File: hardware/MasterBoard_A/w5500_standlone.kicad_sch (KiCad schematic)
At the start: 1 part, among them U18 W5500

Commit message: some progress
w5500 maybe works? shuffled around some more stuff and what not
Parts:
- added C43, C47, C56: 1u, Capacitor_SMD:C_1206_3216Metric_Pad1.33x1.80mm_HandSolder, symbol Device:C_Small
- added C48, C50, C55: 220n, Capacitor_SMD:C_0805_2012Metric_Pad1.18x1.45mm_HandSolder, symbol Device:C_Small
- added C53, C69: 1n 2kV, Capacitor_SMD:C_1206_3216Metric_Pad1.33x1.80mm_HandSolder, symbol Device:C_Small
- added C54: 10u, Capacitor_SMD:C_1206_3216Metric_Pad1.33x1.80mm_HandSolder, symbol Device:C_Small
- added C57: 100n, Capacitor_SMD:C_1206_3216Metric_Pad1.33x1.80mm_HandSolder, symbol Device:C_Small
- added C58, C63, C64: 6.8n, Capacitor_SMD:C_0805_2012Metric_Pad1.18x1.45mm_HandSolder, symbol Device:C_Small
- added C59, C62, C65, C67: 10n, Capacitor_SMD:C_0805_2012Metric_Pad1.18x1.45mm_HandSolder, symbol Device:C_Small
- added C60, C68: 22n, Capacitor_SMD:C_0805_2012Metric_Pad1.18x1.45mm_HandSolder, symbol Device:C_Small
- added C66, C71, C72: 18p, Capacitor_SMD:C_0805_2012Metric_Pad1.18x1.45mm_HandSolder, symbol Device:C_Small
- added C70: 4.7u, Capacitor_SMD:C_0805_2012Metric_Pad1.18x1.45mm_HandSolder, symbol Device:C_Small
- added J10: RJ45_Amphenol_RJMG1BD3B8K1ANR, Connector_RJ:RJ45_Amphenol_RJMG1BD3B8K1ANR, symbol Connector:RJ45_Amphenol_RJMG1BD3B8K1ANR
- added NT1, NT2: NetTie_2, symbol Device:NetTie_2
- added R57: 2.4k, Resistor_SMD:R_0805_2012Metric_Pad1.20x1.40mm_HandSolder, symbol Device:R_Small_US
- added R60, R81, R82: 750, Resistor_SMD:R_1206_3216Metric_Pad1.30x1.75mm_HandSolder, symbol Device:R_Small_US
- added R62: 39k, Resistor_SMD:R_0805_2012Metric_Pad1.20x1.40mm_HandSolder, symbol Device:R_Small_US
- added R63: 3.32k, Resistor_SMD:R_0805_2012Metric_Pad1.20x1.40mm_HandSolder, symbol Device:R_Small_US
- added R64: 97.6k, Resistor_SMD:R_0805_2012Metric_Pad1.20x1.40mm_HandSolder, symbol Device:R_Small_US
- added R65, R72, R73, R78, R79: 49.9, Resistor_SMD:R_0805_2012Metric_Pad1.20x1.40mm_HandSolder, symbol Device:R_Small_US
- added R66: 4.99k, Resistor_SMD:R_1206_3216Metric_Pad1.30x1.75mm_HandSolder, symbol Device:R_Small_US
- added R67: 10k, Resistor_SMD:R_0805_2012Metric_Pad1.20x1.40mm_HandSolder, symbol Device:R_Small_US
- added R68, R80: 10, Resistor_SMD:R_1206_3216Metric_Pad1.30x1.75mm_HandSolder, symbol Device:R_Small_US
- added R69: 121, Resistor_SMD:R_0805_2012Metric_Pad1.20x1.40mm_HandSolder, symbol Device:R_Small_US
- added R70, R87: 226, Resistor_SMD:R_0805_2012Metric_Pad1.20x1.40mm_HandSolder, symbol Device:R_Small_US
- added R71, R74, R75, R76, R77: 3.3, Resistor_SMD:R_1206_3216Metric_Pad1.30x1.75mm_HandSolder, symbol Device:R_Small_US
- added R84: 12.4k, Resistor_SMD:R_0805_2012Metric_Pad1.20x1.40mm_HandSolder, symbol Device:R_Small_US
- added R85, R86: 1M, Resistor_SMD:R_0805_2012Metric_Pad1.20x1.40mm_HandSolder, symbol Device:R_Small_US
- added Y1: 25MHz, Crystal:Crystal_SMD_ECS_CSM3X-2Pin_7.6x4.1mm, symbol Device:Crystal
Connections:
- net at U18.1 (TXN): now also R72.1, R74.2
- net at U18.10 (EXRES1): now also R84.1
- net +3.3VA: now reaches U18.11 (AVDD), U18.15 (AVDD), U18.17 (AVDD), U18.21 (AVDD), U18.4 (AVDD), U18.8 (AVDD)
- net +3.3VA: now also C43.1, C47.1, C48.1, C50.1, NT1.2, R72.2, R73.2, R80.2
- net GNDA: now reaches U18.14 (AGND), U18.16 (AGND), U18.19 (AGND), U18.3 (AGND), U18.48 (AGND), U18.9 (AGND)
- net GNDA: now also C43.2, C47.2, C48.2, C50.2, C62.2, C67.2, C68.2, C69.2, C70.2, NT2.2, R84.2
- net at U18.2 (TXP): now also R73.1, R75.2
- net at U18.20 (TOCAP): now also C70.1
- net at U18.22 (1V2O): now also C65.1
- net at U18.25 (LINKLED): now also R82.1
- net at U18.27 (ACTLED): now also R81.1
- net +3.3V: now reaches U18.28 (VDD)
- net +3.3V: now also J10.L1, J10.L4, NT1.1
- net GND: now reaches U18.29 (GND)
- net GND: now also C65.2, C69.1, C71.2, C72.2, J10.R8, NT2.1
- net at U18.30 (XI/CLKIN): now also R86.1, R87.1
- net at U18.31 (XO): now also C71.1, R86.2, Y1.2
- net at U18.5 (RXN): now also R76.2, R79.2
- net at U18.6 (RXP): now also R77.2, R78.2
- new net: J10.L3, R81.2
- new net: C64.1, R77.1
- new net: C63.1, R76.1
- new net: C67.1, J10.R5 (RCT)
- new net: C68.1, J10.R4 (TCT), R80.1
- new net: C62.1, R78.1, R79.1
- new net: C63.2, J10.R3 (RD+)
- new net: C72.1, R87.2, Y1.1
- new net: J10.R1 (TD+), R74.1
- new net: C64.2, J10.R6 (RD-)
- new net: J10.R2 (TD-), R75.1
- new net: J10.L2, R82.2
- no-connect marks 0 -> 13
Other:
- note added: "- 99% chance does not meet FCC standards"
- note added: "design guide: https://docs.wiznet.io/img/design_guide/Wiznet%20Ethernet%20Design%20Guide_ENG.pdf"
- moved on the sheet: U18

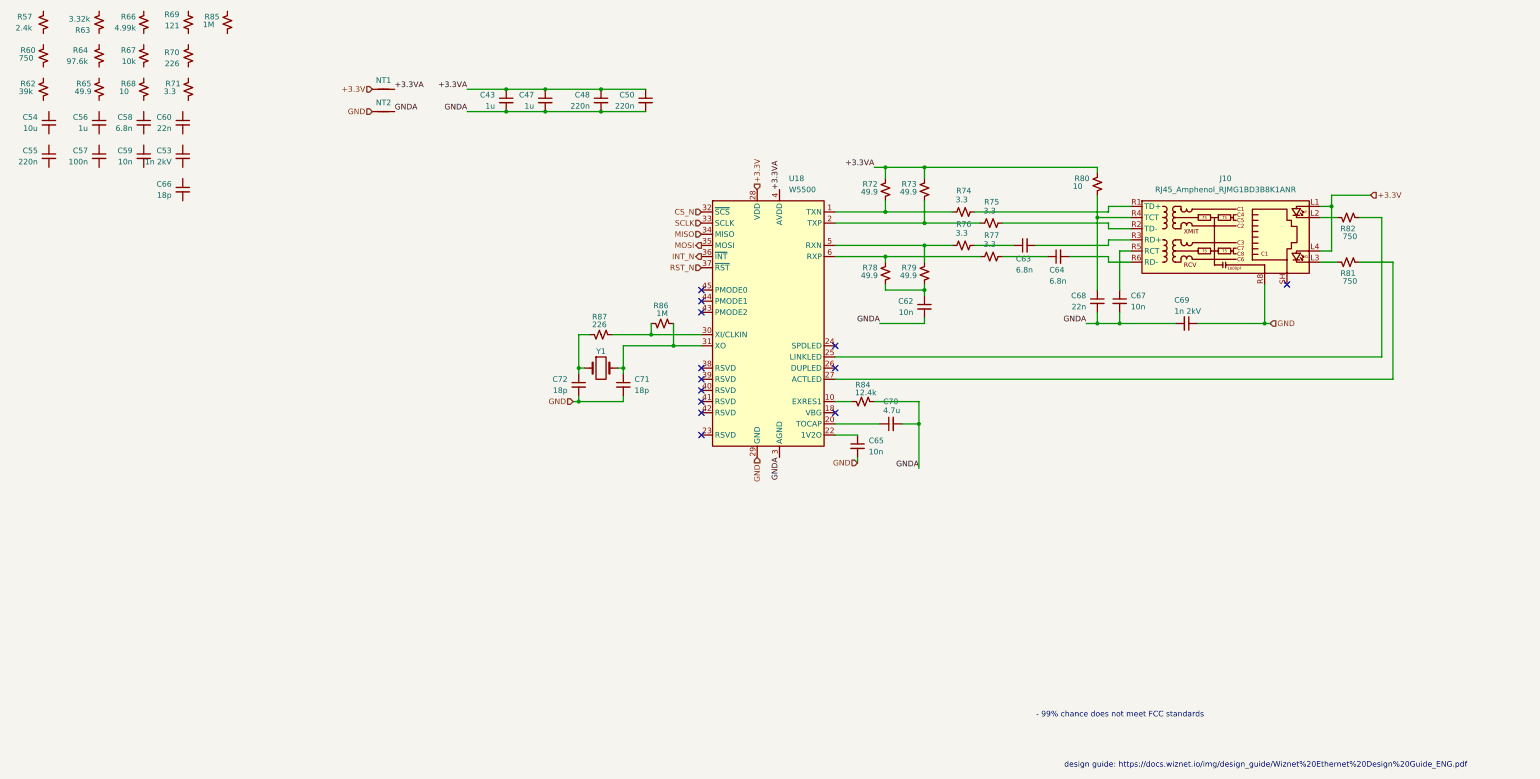
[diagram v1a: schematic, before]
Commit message: near final
missing direct MCU connections, pin map excel sheet needs piddled with. schematic needs reviewed
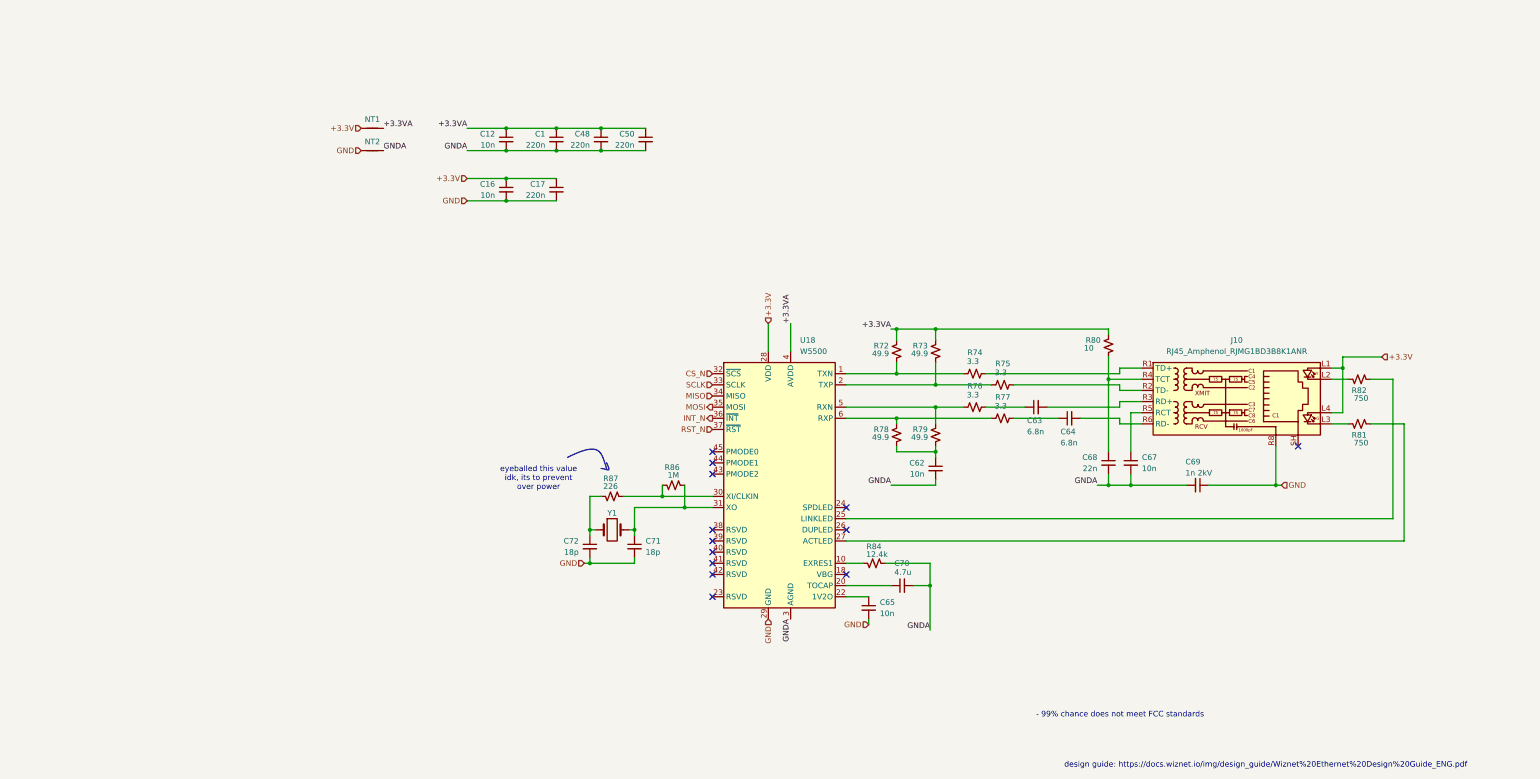
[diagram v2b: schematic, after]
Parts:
- removed C43, C47, C56: 1u, Capacitor_SMD:C_1206_3216Metric_Pad1.33x1.80mm_HandSolder, symbol Device:C_Small
- removed C53: 1n 2kV, Capacitor_SMD:C_1206_3216Metric_Pad1.33x1.80mm_HandSolder, symbol Device:C_Small
- removed C54: 10u, Capacitor_SMD:C_1206_3216Metric_Pad1.33x1.80mm_HandSolder, symbol Device:C_Small
- removed C55: 220n, Capacitor_SMD:C_0805_2012Metric_Pad1.18x1.45mm_HandSolder, symbol Device:C_Small
- removed C57: 100n, Capacitor_SMD:C_1206_3216Metric_Pad1.33x1.80mm_HandSolder, symbol Device:C_Small
- removed C58: 6.8n, Capacitor_SMD:C_0805_2012Metric_Pad1.18x1.45mm_HandSolder, symbol Device:C_Small
- removed C59: 10n, Capacitor_SMD:C_0805_2012Metric_Pad1.18x1.45mm_HandSolder, symbol Device:C_Small
- removed C60: 22n, Capacitor_SMD:C_0805_2012Metric_Pad1.18x1.45mm_HandSolder, symbol Device:C_Small
- removed C66: 18p, Capacitor_SMD:C_0805_2012Metric_Pad1.18x1.45mm_HandSolder, symbol Device:C_Small
- removed R57: 2.4k, Resistor_SMD:R_0805_2012Metric_Pad1.20x1.40mm_HandSolder, symbol Device:R_Small_US
- removed R60: 750, Resistor_SMD:R_1206_3216Metric_Pad1.30x1.75mm_HandSolder, symbol Device:R_Small_US
- removed R62: 39k, Resistor_SMD:R_0805_2012Metric_Pad1.20x1.40mm_HandSolder, symbol Device:R_Small_US
- removed R63: 3.32k, Resistor_SMD:R_0805_2012Metric_Pad1.20x1.40mm_HandSolder, symbol Device:R_Small_US
- removed R64: 97.6k, Resistor_SMD:R_0805_2012Metric_Pad1.20x1.40mm_HandSolder, symbol Device:R_Small_US
- removed R65: 49.9, Resistor_SMD:R_0805_2012Metric_Pad1.20x1.40mm_HandSolder, symbol Device:R_Small_US
- removed R66: 4.99k, Resistor_SMD:R_1206_3216Metric_Pad1.30x1.75mm_HandSolder, symbol Device:R_Small_US
- removed R67: 10k, Resistor_SMD:R_0805_2012Metric_Pad1.20x1.40mm_HandSolder, symbol Device:R_Small_US
- removed R68: 10, Resistor_SMD:R_1206_3216Metric_Pad1.30x1.75mm_HandSolder, symbol Device:R_Small_US
- removed R69: 121, Resistor_SMD:R_0805_2012Metric_Pad1.20x1.40mm_HandSolder, symbol Device:R_Small_US
- removed R70: 226, Resistor_SMD:R_0805_2012Metric_Pad1.20x1.40mm_HandSolder, symbol Device:R_Small_US
- removed R71: 3.3, Resistor_SMD:R_1206_3216Metric_Pad1.30x1.75mm_HandSolder, symbol Device:R_Small_US
- removed R85: 1M, Resistor_SMD:R_0805_2012Metric_Pad1.20x1.40mm_HandSolder, symbol Device:R_Small_US
- added C1, C17: 220n, Capacitor_SMD:C_0805_2012Metric_Pad1.18x1.45mm_HandSolder, symbol Device:C_Small
- added C12, C16: 10n, Capacitor_SMD:C_0805_2012Metric_Pad1.18x1.45mm_HandSolder, symbol Device:C_Small
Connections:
- net +3.3V: now also C16.1, C17.1
- net +3.3VA: now also C1.1, C12.1
- net GND: now also C16.2, C17.2
- net GNDA: now also C1.2, C12.2
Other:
- note added: "eyeballed this value idk, its to prevent over power"
- moved on the sheet: C48, C50, C62, C63, C64, C65, C67, C68, C69, C70, C71, C72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

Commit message: one must have hope
eyeballed the ethernet transmission lines, i think it'll work. absolute pain without using footprints smaller than 0805 but it think itll be fine. also shuffled together the PWM sig bank
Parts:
- added C3, C46, C51: 220n, Capacitor_SMD:C_0805_2012Metric_Pad1.18x1.45mm_HandSolder, symbol Device:C_Small
- added C47: 10n, Capacitor_SMD:C_0805_2012Metric_Pad1.18x1.45mm_HandSolder, symbol Device:C_Small
- added C54: 10u, Capacitor_SMD:C_1206_3216Metric_Pad1.33x1.80mm_HandSolder, symbol Device:C_Small
- C12: value 10n -> 220n; mouser https://www.mouser.com/ProductDetail/KYOCERA-AVX/08051C103J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 -> https://www.mouser.com/ProductDetail/Samsung-Electro-Mechan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; specs 10nF, 5%, 100VDC, X7R, MLCC -> 100VDC, X7R, 10%, -55C, +125C, 220nF; unit x1 0.10 -> (none); unit x10 0.04 -> 0.054
- NT1, NT2: footprint (none) -> NetTie:NetTie-2_SMD_Pad2.0mm
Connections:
- net +3.3V: now also C3.1
- net +3.3VA: now also C46.1, C47.1, C51.1, C54.1
- net GND: now also C3.2
- net GNDA: now also C46.2, C47.2, C51.2, C54.2
- net RX_1-: now reaches C64.1, R77.1
- net RX-: now reaches R77.2, R78.2, U18.6 (RXP)
- net TX+: now reaches R72.1, R74.2, U18.1 (TXN)
- net TX-: now reaches R73.1, R75.2, U18.2 (TXP)
- net RX+: now reaches R76.2, R79.2, U18.5 (RXN)
- net RX_1+: now reaches C63.1, R76.1
- net RD+: now reaches C63.2, J10.R3 (RD+)
- net TD+: now reaches J10.R1 (TD+), R74.1
- net RD-: now reaches C64.2, J10.R6 (RD-)
- net TD-: now reaches J10.R2 (TD-), R75.1
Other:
- moved on the sheet: C63

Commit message: all but MCU
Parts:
- added C55: 10n, Capacitor_SMD:C_0805_2012Metric_Pad1.18x1.45mm_HandSolder, symbol Device:C_Small
- added C56: 220n, Capacitor_SMD:C_0805_2012Metric_Pad1.18x1.45mm_HandSolder, symbol Device:C_Small
- added C57: 10u, Capacitor_SMD:C_1206_3216Metric_Pad1.33x1.80mm_HandSolder, symbol Device:C_Small
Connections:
- net +3.3V: now also C55.1, C56.1, C57.1
- net GND: now also C55.2, C56.2, C57.2

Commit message: up to date meta sheet and made release files
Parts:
- C1, C12, C17, C3, C46, C48, C50, C51, C56: unit x1 (none) -> 0.054
- U18: mouser (none) -> https://www.mouser.com/ProductDetail/WIZnet/W5500?qs=2vh%25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; unit x1 (none) -> 3.67; unit x10 (none) -> 2.77
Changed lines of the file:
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@@
 			)
 		)
+		(property "mouser" "https://www.mouser.com/ProductDetail/WIZnet/W5500?qs=2vh%252B45pPFtzthUpYPd4pqA%3D%3D&srsltid=AfmBOooS_FwSksJzNIrEWxsXr2WyGB4jGlrzDUdR5nOADXI-EfhrY8FA"
+			(at 119.38 115.57 0)
+			(effects
+				(font
+					(size 1.27 1.27)
+				)
+				(hide yes)
+			)
+		)
+		(property "unit x10" "2.77"
+			(at 119.38 115.57 0)
+			(effects
+				(font
+					(size 1.27 1.27)
+				)
+				(hide yes)
+			)
+		)
+		(property "unit x1" "3.67"
+			(at 119.38 115.57 0)
+			(effects
+				(font
+					(size 1.27 1.27)
+				)
+				(hide yes)
+			)
+		)
 		(pin "31"
 		)
@@
 			)
 		)
+		(property "unit x1" "0.054"
+			(at 124.46 73.66 0)
+			(effects
+				(font
+					(size 1.27 1.27)
+				)
+				(hide yes)
+			)
+		)
 		(pin "2"
 		)
@@
 			)
 		)
+		(property "unit x1" "0.054"
+			(at 90.17 48.26 0)
+			(effects
+				(font
+					(size 1.27 1.27)
+				)
+				(hide yes)
+			)
+		)
 		(pin "2"
 		)
@@
 			)
 		)
+		(property "unit x1" "0.054"
+			(at 78.74 36.83 0)
+			(effects
+				(font
+					(size 1.27 1.27)
+				)
+				(hide yes)
+			)
+		)
 		(pin "2"
 		)
@@
 			)
 		)
+		(property "unit x1" "0.054"
+			(at 111.76 36.83 0)
+			(effects
+				(font
+					(size 1.27 1.27)
+				)
+				(hide yes)
+			)
+		)
 		(pin "2"
 		)
@@
 			)
 		)
+		(property "unit x1" "0.054"
+			(at 114.3 73.66 0)
+			(effects
+				(font
+					(size 1.27 1.27)
+				)
+				(hide yes)
+			)
+		)
 		(pin "2"
 		)
@@
 			)
 		)
+		(property "unit x1" "0.054"
+			(at 68.58 48.26 0)
+			(effects
+				(font
+					(size 1.27 1.27)
+				)
+				(hide yes)
+			)
+		)
 		(pin "2"
 		)
@@
 			)
 		)
+		(property "unit x1" "0.054"
+			(at 88.9 36.83 0)
+			(effects
+				(font
+					(size 1.27 1.27)
+				)
+				(hide yes)
+			)
+		)
 		(pin "2"
 		)
@@
 			)
 		)
+		(property "unit x1" "0.054"
+			(at 58.42 36.83 0)
+			(effects
+				(font
+					(size 1.27 1.27)
+				)
+				(hide yes)
+			)
+		)
 		(pin "2"
 		)
@@
 			(at 68.58 36.83 0)
 			(effects
+				(font
+					(size 1.27 1.27)
+				)
+				(hide yes)
+			)
+		)
+		(property "unit x1" "0.054"
+			(at 68.58 36.83 0)
+			(effects
